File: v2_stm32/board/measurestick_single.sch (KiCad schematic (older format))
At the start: 4 parts, among them IC1 LM393, J9 USB_A

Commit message: More PCB design
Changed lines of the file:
@@
 AR Path="/60265FC9/60261634" Ref="IC3"  Part="2"
 AR Path="/6026601C/60261634" Ref="IC4"  Part="2"
-F 0 "IC1" H 3850 3817 50  0000 C CNN
+F 0 "IC4" H 3850 3817 50  0000 C CNN
 F 1 "LM393" H 3850 3726 50  0000 C CNN
 F 2 "Package_SO:SOIC-8_3.9x4.9mm_P1.27mm" H 3850 3450 50  0001 C CNN
@@
 AR Path="/60265FC9/6026163B" Ref="IC3"  Part="1"
 AR Path="/6026601C/6026163B" Ref="IC4"  Part="1"
-F 0 "IC1" H 3850 3067 50  0000 C CNN
+F 0 "IC4" H 3850 3067 50  0000 C CNN
 F 1 "LM393" H 3850 2976 50  0000 C CNN
 F 2 "Package_SO:SOIC-8_3.9x4.9mm_P1.27mm" H 3850 2700 50  0001 C CNN
@@
 AR Path="/60265FC9/60261641" Ref="IC3"  Part="3"
 AR Path="/6026601C/60261641" Ref="IC4"  Part="3"
-F 0 "IC1" H 4908 3096 50  0000 L CNN
+F 0 "IC4" H 4908 3096 50  0000 L CNN
 F 1 "LM393" H 4908 3005 50  0000 L CNN
 F 2 "Package_SO:SOIC-8_3.9x4.9mm_P1.27mm" H 4950 3050 50  0001 C CNN
@@
 AR Path="/6026601C/60261659" Ref="J12"  Part="1"
 AR Path="/60261659" Ref="J?"  Part="1"
-F 0 "J9" H 2407 3467 50  0000 C CNN
+F 0 "J12" H 2407 3467 50  0000 C CNN
 F 1 "USB_A" H 2407 3376 50  0000 C CNN
 F 2 "Lathecontrol_STM32:USB_A_Upright_C26235" H 2500 2950 50  0001 C CNN
@@
 AR Path="/60265FC9/6026167C" Ref="R9"  Part="1"
 AR Path="/6026601C/6026167C" Ref="R11"  Part="1"
-F 0 "R5" H 3470 2346 50  0000 L CNN
+F 0 "R11" H 3470 2346 50  0000 L CNN
 F 1 "13k" H 3470 2255 50  0000 L CNN
 F 2 "Resistor_SMD:R_0603_1608Metric" V 3330 2300 50  0001 C CNN
@@
 AR Path="/60265FC9/60261683" Ref="R10"  Part="1"
 AR Path="/6026601C/60261683" Ref="R12"  Part="1"
-F 0 "R6" H 3470 3796 50  0000 L CNN
+F 0 "R12" H 3470 3796 50  0000 L CNN
 F 1 "3k3" H 3470 3705 50  0000 L CNN
 F 2 "Resistor_SMD:R_0603_1608Metric" V 3330 3750 50  0001 C CNN

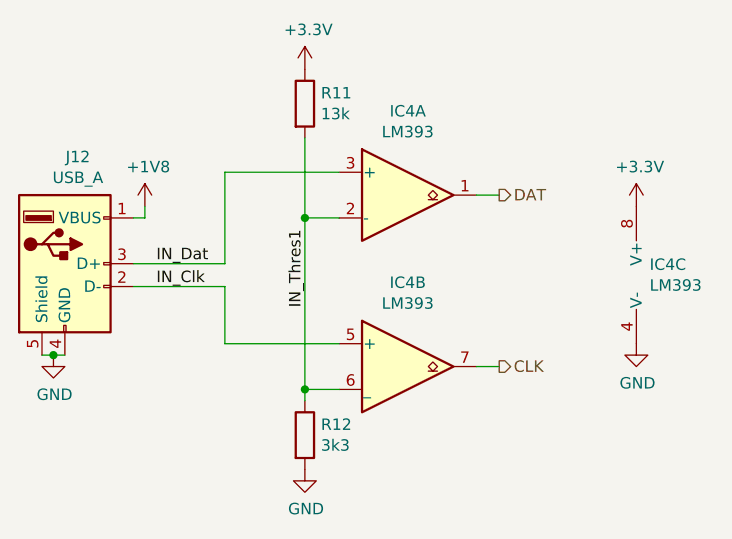
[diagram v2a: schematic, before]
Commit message: Moved to 4 layer PCB. More routing
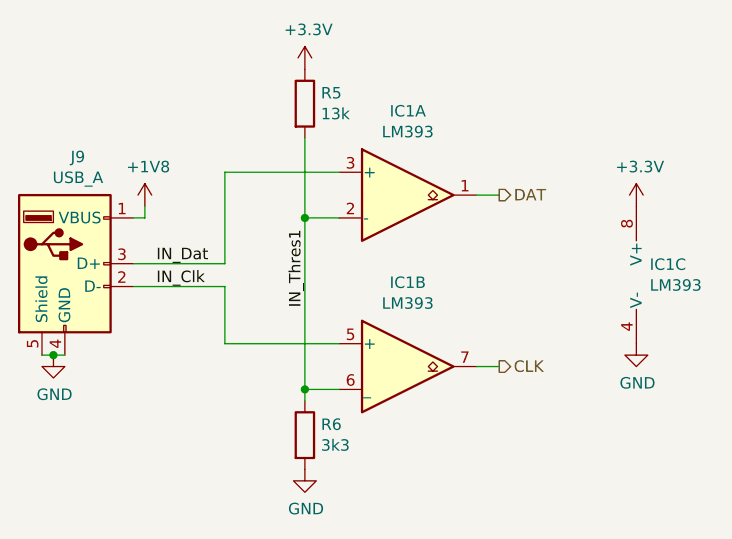
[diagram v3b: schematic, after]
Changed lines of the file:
@@
 AR Path="/60265FC9/60261634" Ref="IC3"  Part="2"
 AR Path="/6026601C/60261634" Ref="IC4"  Part="2"
-F 0 "IC4" H 3850 3817 50  0000 C CNN
+F 0 "IC1" H 3850 3817 50  0000 C CNN
 F 1 "LM393" H 3850 3726 50  0000 C CNN
 F 2 "Package_SO:SOIC-8_3.9x4.9mm_P1.27mm" H 3850 3450 50  0001 C CNN
@@
 AR Path="/60265FC9/6026163B" Ref="IC3"  Part="1"
 AR Path="/6026601C/6026163B" Ref="IC4"  Part="1"
-F 0 "IC4" H 3850 3067 50  0000 C CNN
+F 0 "IC1" H 3850 3067 50  0000 C CNN
 F 1 "LM393" H 3850 2976 50  0000 C CNN
 F 2 "Package_SO:SOIC-8_3.9x4.9mm_P1.27mm" H 3850 2700 50  0001 C CNN
@@
 AR Path="/60265FC9/60261641" Ref="IC3"  Part="3"
 AR Path="/6026601C/60261641" Ref="IC4"  Part="3"
-F 0 "IC4" H 4908 3096 50  0000 L CNN
+F 0 "IC1" H 4908 3096 50  0000 L CNN
 F 1 "LM393" H 4908 3005 50  0000 L CNN
 F 2 "Package_SO:SOIC-8_3.9x4.9mm_P1.27mm" H 4950 3050 50  0001 C CNN
@@
 AR Path="/60265FC9/60261649" Ref="#PWR058"  Part="1"
 AR Path="/6026601C/60261649" Ref="#PWR066"  Part="1"
-F 0 "#PWR066" H 4850 3100 50  0001 C CNN
+F 0 "#PWR042" H 4850 3100 50  0001 C CNN
 F 1 "GND" H 4855 3177 50  0000 C CNN
 F 2 "" H 4850 3350 50  0001 C CNN
@@
 AR Path="/6026601C/60261659" Ref="J12"  Part="1"
 AR Path="/60261659" Ref="J?"  Part="1"
-F 0 "J12" H 2407 3467 50  0000 C CNN
+F 0 "J9" H 2407 3467 50  0000 C CNN
 F 1 "USB_A" H 2407 3376 50  0000 C CNN
 F 2 "Lathecontrol_STM32:USB_A_Upright_C26235" H 2500 2950 50  0001 C CNN
@@
 AR Path="/60265FC9/60261663" Ref="#PWR053"  Part="1"
 AR Path="/6026601C/60261663" Ref="#PWR061"  Part="1"
-F 0 "#PWR061" H 2300 3150 50  0001 C CNN
+F 0 "#PWR037" H 2300 3150 50  0001 C CNN
 F 1 "GND" H 2305 3227 50  0000 C CNN
 F 2 "" H 2300 3400 50  0001 C CNN
@@
 AR Path="/60265FC9/6026166C" Ref="#PWR054"  Part="1"
 AR Path="/6026601C/6026166C" Ref="#PWR062"  Part="1"
-F 0 "#PWR062" H 2700 2600 50  0001 C CNN
+F 0 "#PWR038" H 2700 2600 50  0001 C CNN
 F 1 "+1V8" H 2715 2923 50  0000 C CNN
 F 2 "" H 2700 2750 50  0001 C CNN
@@
 AR Path="/60265FC9/6026167C" Ref="R9"  Part="1"
 AR Path="/6026601C/6026167C" Ref="R11"  Part="1"
-F 0 "R11" H 3470 2346 50  0000 L CNN
+F 0 "R5" H 3470 2346 50  0000 L CNN
 F 1 "13k" H 3470 2255 50  0000 L CNN
 F 2 "Resistor_SMD:R_0603_1608Metric" V 3330 2300 50  0001 C CNN
@@
 AR Path="/60265FC9/60261683" Ref="R10"  Part="1"
 AR Path="/6026601C/60261683" Ref="R12"  Part="1"
-F 0 "R12" H 3470 3796 50  0000 L CNN
+F 0 "R6" H 3470 3796 50  0000 L CNN
 F 1 "3k3" H 3470 3705 50  0000 L CNN
 F 2 "Resistor_SMD:R_0603_1608Metric" V 3330 3750 50  0001 C CNN
@@
 AR Path="/60265FC9/60261690" Ref="#PWR055"  Part="1"
 AR Path="/6026601C/60261690" Ref="#PWR063"  Part="1"
-F 0 "#PWR063" H 3400 2000 50  0001 C CNN
+F 0 "#PWR039" H 3400 2000 50  0001 C CNN
 F 1 "+3.3V" H 3415 2323 50  0000 C CNN
 F 2 "" H 3400 2150 50  0001 C CNN
@@
 AR Path="/60265FC9/60261696" Ref="#PWR056"  Part="1"
 AR Path="/6026601C/60261696" Ref="#PWR064"  Part="1"
-F 0 "#PWR064" H 3400 3650 50  0001 C CNN
+F 0 "#PWR040" H 3400 3650 50  0001 C CNN
 F 1 "GND" H 3405 3727 50  0000 C CNN
 F 2 "" H 3400 3900 50  0001 C CNN
@@
 AR Path="/60265FC9/60261675" Ref="#PWR057"  Part="1"
 AR Path="/6026601C/60261675" Ref="#PWR065"  Part="1"
-F 0 "#PWR065" H 4850 2600 50  0001 C CNN
+F 0 "#PWR041" H 4850 2600 50  0001 C CNN
 F 1 "+3.3V" H 4865 2923 50  0000 C CNN
 F 2 "" H 4850 2750 50  0001 C CNN

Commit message: Started current loop output for frequency converter
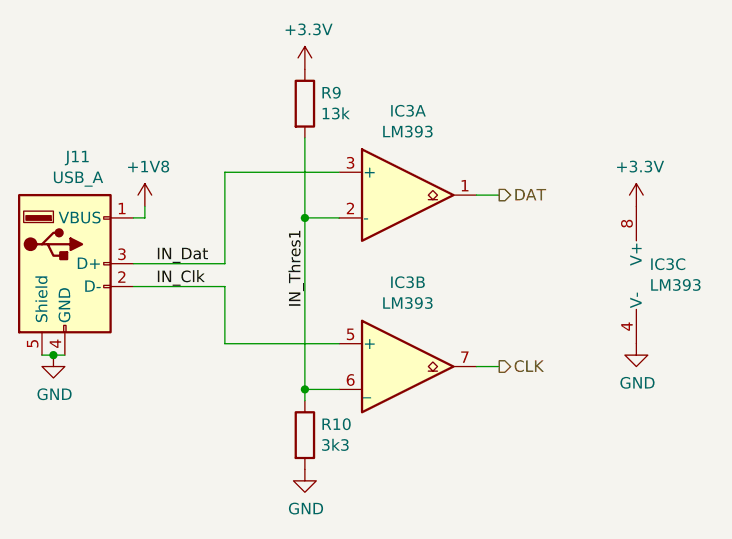
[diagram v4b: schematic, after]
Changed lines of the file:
@@
 $Descr A4 11693 8268
 encoding utf-8
-Sheet 2 7
+Sheet 4 8
 Title ""
 Date ""
@@
 AR Path="/60265FC9/60261634" Ref="IC3"  Part="2"
 AR Path="/6026601C/60261634" Ref="IC4"  Part="2"
-F 0 "IC1" H 3850 3817 50  0000 C CNN
+F 0 "IC3" H 3850 3817 50  0000 C CNN
 F 1 "LM393" H 3850 3726 50  0000 C CNN
 F 2 "Package_SO:SOIC-8_3.9x4.9mm_P1.27mm" H 3850 3450 50  0001 C CNN
@@
 AR Path="/60265FC9/6026163B" Ref="IC3"  Part="1"
 AR Path="/6026601C/6026163B" Ref="IC4"  Part="1"
-F 0 "IC1" H 3850 3067 50  0000 C CNN
+F 0 "IC3" H 3850 3067 50  0000 C CNN
 F 1 "LM393" H 3850 2976 50  0000 C CNN
 F 2 "Package_SO:SOIC-8_3.9x4.9mm_P1.27mm" H 3850 2700 50  0001 C CNN
@@
 AR Path="/60265FC9/60261641" Ref="IC3"  Part="3"
 AR Path="/6026601C/60261641" Ref="IC4"  Part="3"
-F 0 "IC1" H 4908 3096 50  0000 L CNN
+F 0 "IC3" H 4908 3096 50  0000 L CNN
 F 1 "LM393" H 4908 3005 50  0000 L CNN
 F 2 "Package_SO:SOIC-8_3.9x4.9mm_P1.27mm" H 4950 3050 50  0001 C CNN
@@
 AR Path="/60265FC9/60261649" Ref="#PWR058"  Part="1"
 AR Path="/6026601C/60261649" Ref="#PWR066"  Part="1"
-F 0 "#PWR042" H 4850 3100 50  0001 C CNN
+F 0 "#PWR058" H 4850 3100 50  0001 C CNN
 F 1 "GND" H 4855 3177 50  0000 C CNN
 F 2 "" H 4850 3350 50  0001 C CNN
@@
 AR Path="/6026601C/60261659" Ref="J12"  Part="1"
 AR Path="/60261659" Ref="J?"  Part="1"
-F 0 "J9" H 2407 3467 50  0000 C CNN
+F 0 "J11" H 2407 3467 50  0000 C CNN
 F 1 "USB_A" H 2407 3376 50  0000 C CNN
 F 2 "Lathecontrol_STM32:USB_A_Upright_C26235" H 2500 2950 50  0001 C CNN
@@
 AR Path="/60265FC9/60261663" Ref="#PWR053"  Part="1"
 AR Path="/6026601C/60261663" Ref="#PWR061"  Part="1"
-F 0 "#PWR037" H 2300 3150 50  0001 C CNN
+F 0 "#PWR053" H 2300 3150 50  0001 C CNN
 F 1 "GND" H 2305 3227 50  0000 C CNN
 F 2 "" H 2300 3400 50  0001 C CNN
@@
 AR Path="/60265FC9/6026166C" Ref="#PWR054"  Part="1"
 AR Path="/6026601C/6026166C" Ref="#PWR062"  Part="1"
-F 0 "#PWR038" H 2700 2600 50  0001 C CNN
+F 0 "#PWR054" H 2700 2600 50  0001 C CNN
 F 1 "+1V8" H 2715 2923 50  0000 C CNN
 F 2 "" H 2700 2750 50  0001 C CNN
@@
 AR Path="/60265FC9/6026167C" Ref="R9"  Part="1"
 AR Path="/6026601C/6026167C" Ref="R11"  Part="1"
-F 0 "R5" H 3470 2346 50  0000 L CNN
+F 0 "R9" H 3470 2346 50  0000 L CNN
 F 1 "13k" H 3470 2255 50  0000 L CNN
 F 2 "Resistor_SMD:R_0603_1608Metric" V 3330 2300 50  0001 C CNN
@@
 AR Path="/60265FC9/60261683" Ref="R10"  Part="1"
 AR Path="/6026601C/60261683" Ref="R12"  Part="1"
-F 0 "R6" H 3470 3796 50  0000 L CNN
+F 0 "R10" H 3470 3796 50  0000 L CNN
 F 1 "3k3" H 3470 3705 50  0000 L CNN
 F 2 "Resistor_SMD:R_0603_1608Metric" V 3330 3750 50  0001 C CNN
@@
 AR Path="/60265FC9/60261690" Ref="#PWR055"  Part="1"
 AR Path="/6026601C/60261690" Ref="#PWR063"  Part="1"
-F 0 "#PWR039" H 3400 2000 50  0001 C CNN
+F 0 "#PWR055" H 3400 2000 50  0001 C CNN
 F 1 "+3.3V" H 3415 2323 50  0000 C CNN
 F 2 "" H 3400 2150 50  0001 C CNN
@@
 AR Path="/60265FC9/60261696" Ref="#PWR056"  Part="1"
 AR Path="/6026601C/60261696" Ref="#PWR064"  Part="1"
-F 0 "#PWR040" H 3400 3650 50  0001 C CNN
+F 0 "#PWR056" H 3400 3650 50  0001 C CNN
 F 1 "GND" H 3405 3727 50  0000 C CNN
 F 2 "" H 3400 3900 50  0001 C CNN
@@
 AR Path="/60265FC9/60261675" Ref="#PWR057"  Part="1"
 AR Path="/6026601C/60261675" Ref="#PWR065"  Part="1"
-F 0 "#PWR041" H 4850 2600 50  0001 C CNN
+F 0 "#PWR057" H 4850 2600 50  0001 C CNN
 F 1 "+3.3V" H 4865 2923 50  0000 C CNN
 F 2 "" H 4850 2750 50  0001 C CNN
